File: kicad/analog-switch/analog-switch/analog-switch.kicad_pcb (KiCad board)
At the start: 2 copper layers, 17.8 x 43.2 mm, 11 parts, among them J1 Conn_01x04, J2 Conn_01x16_MountingPin, J4 Conn_01x04, J5 Conn_01x16_MountingPin, Q1 Q_PNP_EBC, U1 CD74HC4067M, U2 74HC595, U3 CD74HC4067M

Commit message: proj settings
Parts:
- J1: value Conn_01x04 -> Conn_01x05_Male; footprint Connector_PinHeader_2.54mm:PinHeader_1x04_P2.54mm_Vertical -> Connector_PinHeader_2.00mm:PinHeader_1x05_P2.00mm_Vertical
- J2, J5: value Conn_01x16_MountingPin -> Conn_01x17_Male; footprint Connector_PinHeader_2.54mm:PinHeader_1x16_P2.54mm_Vertical -> Connector_PinHeader_2.54mm:PinHeader_1x17_P2.54mm_Vertical
- J4: value Conn_01x04 -> Conn_01x03_Female; footprint Connector_PinHeader_2.54mm:PinHeader_1x04_P2.54mm_Vertical -> Connector_PinHeader_2.00mm:PinHeader_1x03_P2.00mm_Vertical
- U1: moved to B.Cu
- moved R1 40.9 mm to (82.4, 66.0)
- moved R3 27.7 mm to (82.4, 64.3), turned to 180 degrees
- moved Q1 10.5 mm to (82.8, 69.6)
- moved U3 4.10 mm to (59.4, 63.8)
- moved J4 3.89 mm to (60.2, 52.3)
- moved U1 3.64 mm to (59.2, 68.3), turned to -90 degrees
- moved J1 0.79 mm to (56.2, 93.0)
- moved J5 0.71 mm to (67.8, 52.6)
- moved U2 0.25 mm to (60.2, 85.1), turned to -90 degrees
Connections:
- J1 pad 1: Net-(J1-Pad1) -> AN1
- J1 pad 2: Net-(J1-Pad2) -> AN2
- J1 pad 4: GND -> Net-(J1-Pad4)
- J4 pad 3: Net-(J1-Pad3) -> Net-(J1-Pad5)
- R1 pad 2: Net-(J1-Pad3) -> Net-(J1-Pad5)
- R2 pad 1: Net-(J1-Pad3) -> Net-(Q1-Pad2)
- R2 pad 2: Net-(Q1-Pad2) -> Net-(J1-Pad5)
- R3 pad 1: Net-(Q1-Pad3) -> GND
- R3 pad 2: GND -> Net-(Q1-Pad3)
- U1 pad 1: Net-(J3-Pada1) -> AN1
- U2 pad 11: Net-(J1-Pad2) -> Net-(J1-Pad4)
- U2 pad 13: Net-(J1-Pad3) -> Net-(J1-Pad5)
- U2 pad 14: Net-(J1-Pad1) -> Net-(J1-Pad3)
- U3 pad 1: Net-(J3-Padb1) -> AN2
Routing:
- net Net-(J5-Pad1): track 0.00 -> 14.1 mm
- net Net-(J5-Pad2): track 0.00 -> 11.6 mm
- net Net-(J5-Pad3): track 0.00 -> 9.70 mm
- net Net-(J5-Pad5): track 0.00 -> 9.37 mm
- net Net-(J5-Pad4): track 0.00 -> 9.26 mm
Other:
- board size 17.8 x 43.2 mm -> 18.9 x 44.2 mm

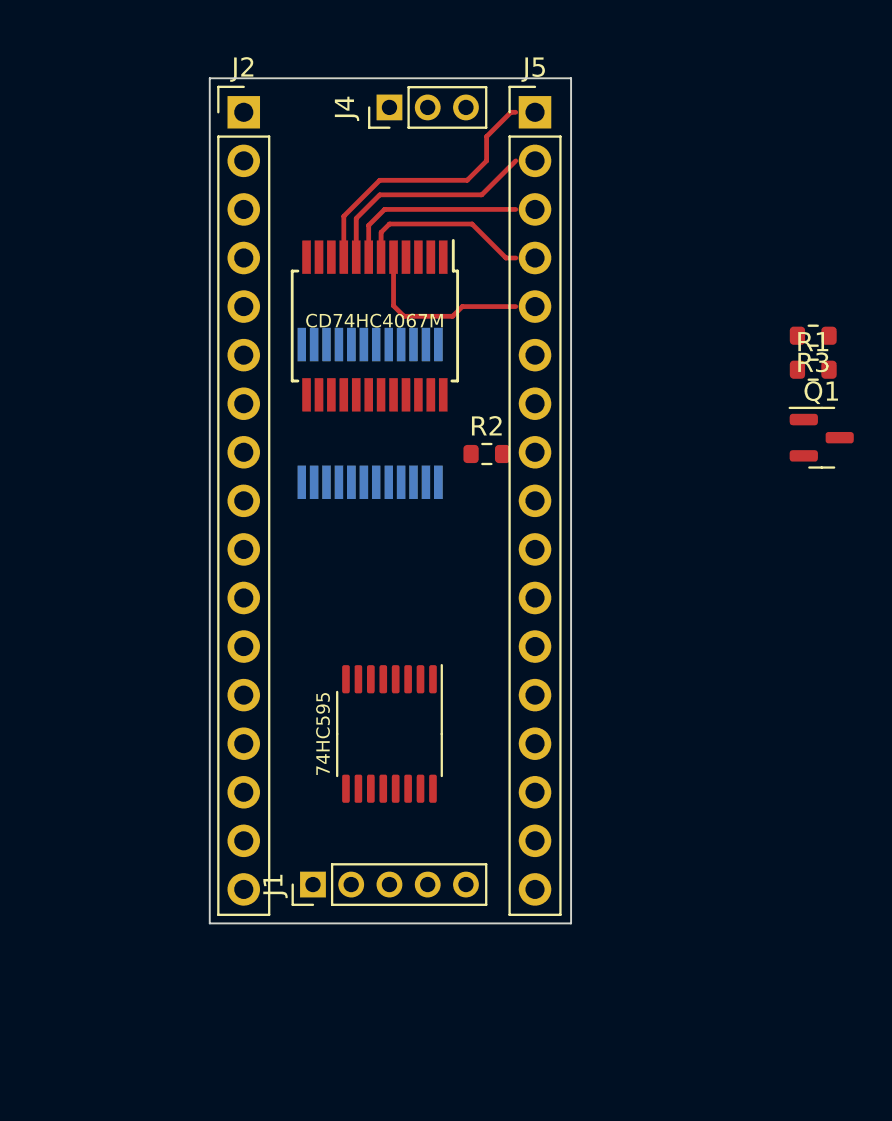
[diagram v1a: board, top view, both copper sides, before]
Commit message: make analog-sw to DIP-40
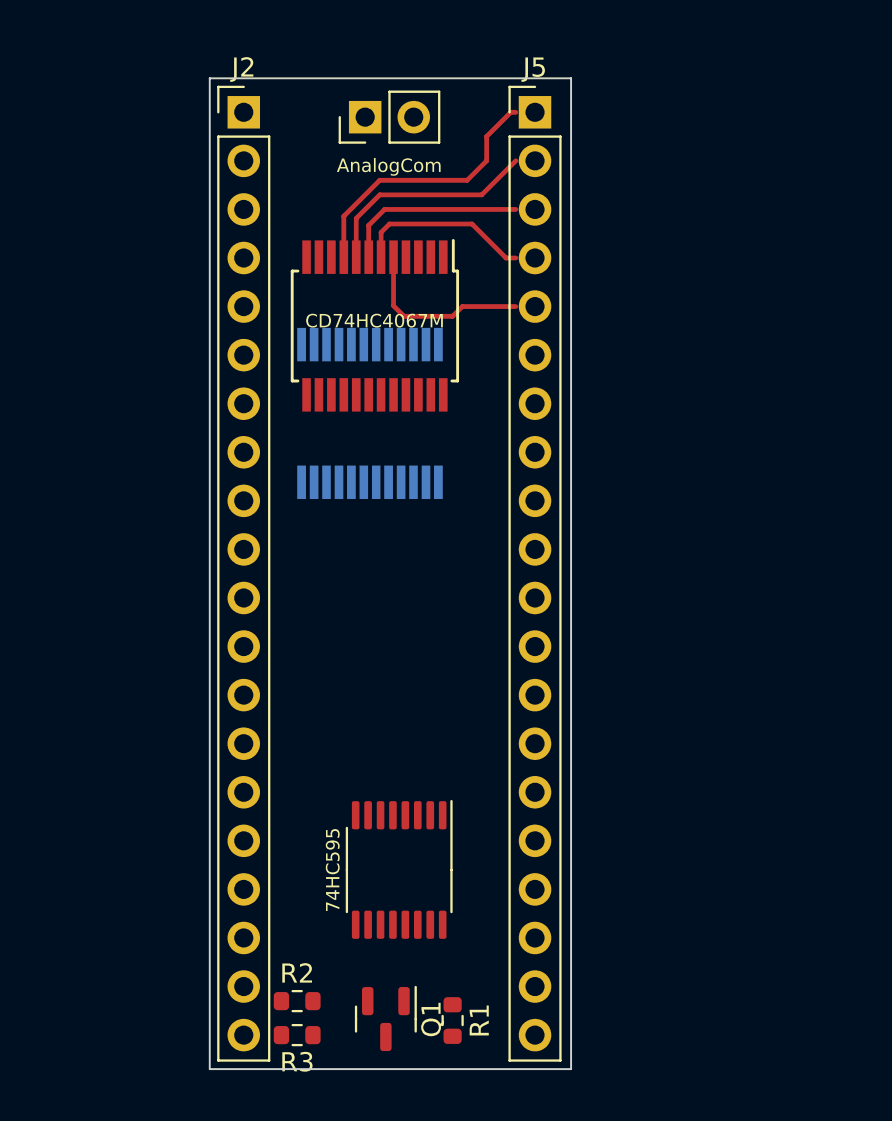
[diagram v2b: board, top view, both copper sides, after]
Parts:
- removed J1: Conn_01x05_Male, Connector_PinHeader_2.00mm:PinHeader_1x05_P2.00mm_Vertical
- removed J4: Conn_01x03_Female, Connector_PinHeader_2.00mm:PinHeader_1x03_P2.00mm_Vertical
- added JP1: AnalogCom, Connector_PinHeader_2.54mm:PinHeader_1x02_P2.54mm_Vertical, F.Cu at (58.9, 52.8)
- J2, J5: value Conn_01x17_Male -> Conn_01x20_Male; footprint Connector_PinHeader_2.54mm:PinHeader_1x17_P2.54mm_Vertical -> Connector_PinHeader_2.54mm:PinHeader_1x20_P2.54mm_Vertical
- moved R3 45.5 mm to (55.4, 100.8)
- moved R1 38.9 mm to (63.5, 100.1), turned to -90 degrees
- moved Q1 38.0 mm to (60.0, 100.0), turned to -90 degrees
- moved R2 30.3 mm to (55.4, 99.1)
- moved U2 7.13 mm to (60.7, 92.2)
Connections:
- J2 pad 17: GND -> Data
- J5 pad 1: Net-(J5-Pad1) -> AN2
- J5 pad 17: +5V -> Net-(J5-Pad17)
- Q1 pad 3: Net-(Q1-Pad3) -> /OE
- R1 pad 2: Net-(J1-Pad5) -> Net-(Q1-Pad2)
- R2 pad 1: Net-(Q1-Pad2) -> /OE
- R2 pad 2: Net-(J1-Pad5) -> Net-(Q1-Pad2)
- R3 pad 2: Net-(Q1-Pad3) -> /OE
- U1 pad 15: Net-(Q1-Pad3) -> /OE
- U2 pad 11: Net-(J1-Pad4) -> Clk
- U2 pad 12: Net-(J4-Pad2) -> ClkH
- U2 pad 13: Net-(J1-Pad5) -> /OE
- U2 pad 14: Net-(J1-Pad3) -> Data
- U2 pad 9: Net-(J4-Pad1) -> DataH
- U3 pad 15: Net-(Q1-Pad3) -> /OE
- U3 pad 16: Net-(J5-Pad16) -> Net-(J5-Pad17)
- U3 pad 17: Net-(J5-Pad15) -> Net-(J5-Pad16)
- U3 pad 18: Net-(J5-Pad14) -> Net-(J5-Pad15)
- U3 pad 19: Net-(J5-Pad13) -> Net-(J5-Pad14)
- U3 pad 2: Net-(J5-Pad8) -> Net-(J5-Pad9)
- U3 pad 20: Net-(J5-Pad12) -> Net-(J5-Pad13)
- U3 pad 21: Net-(J5-Pad11) -> Net-(J5-Pad12)
- U3 pad 22: Net-(J5-Pad10) -> Net-(J5-Pad11)
- U3 pad 23: Net-(J5-Pad9) -> Net-(J5-Pad10)
- U3 pad 3: Net-(J5-Pad7) -> Net-(J5-Pad8)
- U3 pad 4: Net-(J5-Pad6) -> Net-(J5-Pad7)
- U3 pad 5: Net-(J5-Pad5) -> Net-(J5-Pad6)
- U3 pad 6: Net-(J5-Pad4) -> Net-(J5-Pad5)
- U3 pad 7: Net-(J5-Pad3) -> Net-(J5-Pad4)
- U3 pad 8: Net-(J5-Pad2) -> Net-(J5-Pad3)
- U3 pad 9: Net-(J5-Pad1) -> Net-(J5-Pad2)
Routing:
- net Net-(J5-Pad1): track 14.1 -> 0.00 mm
- net Net-(J5-Pad6): track 0.00 -> 9.37 mm
- net Net-(J5-Pad2): track 11.6 -> 14.1 mm
- net Net-(J5-Pad3): track 9.70 -> 11.6 mm
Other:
- board size 18.9 x 44.2 mm -> 18.9 x 51.8 mm
